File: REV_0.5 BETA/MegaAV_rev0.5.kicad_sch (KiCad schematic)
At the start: 167 parts, among them CN1 MD-90SM_MD2, P1 SMD_Conn_01x01, U1 4070, U2 74HCT123, U3 TS924, U4 THS7374, U5 ICS501, U6 TS922, U7 TS924, U8 AD725

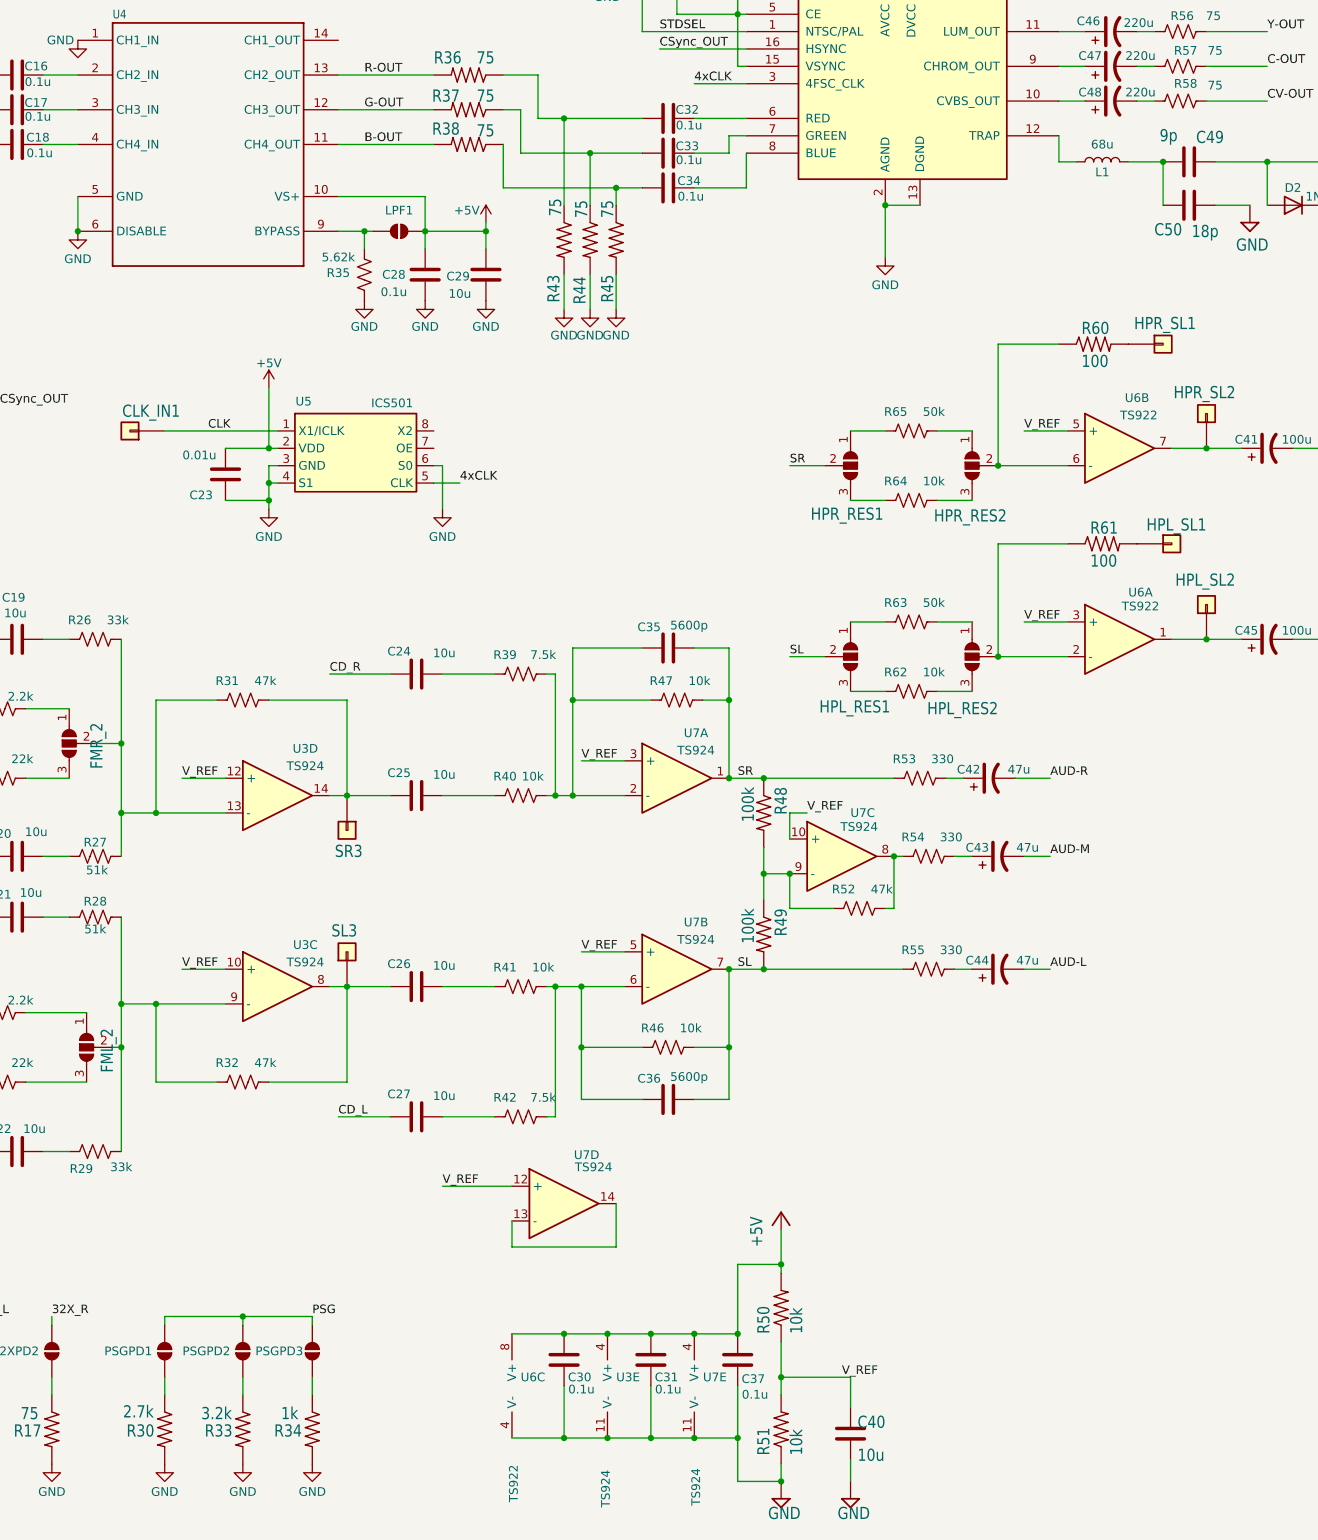
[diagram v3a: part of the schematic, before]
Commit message: optimized luma trap values & PSG fix. Some silscreening to.
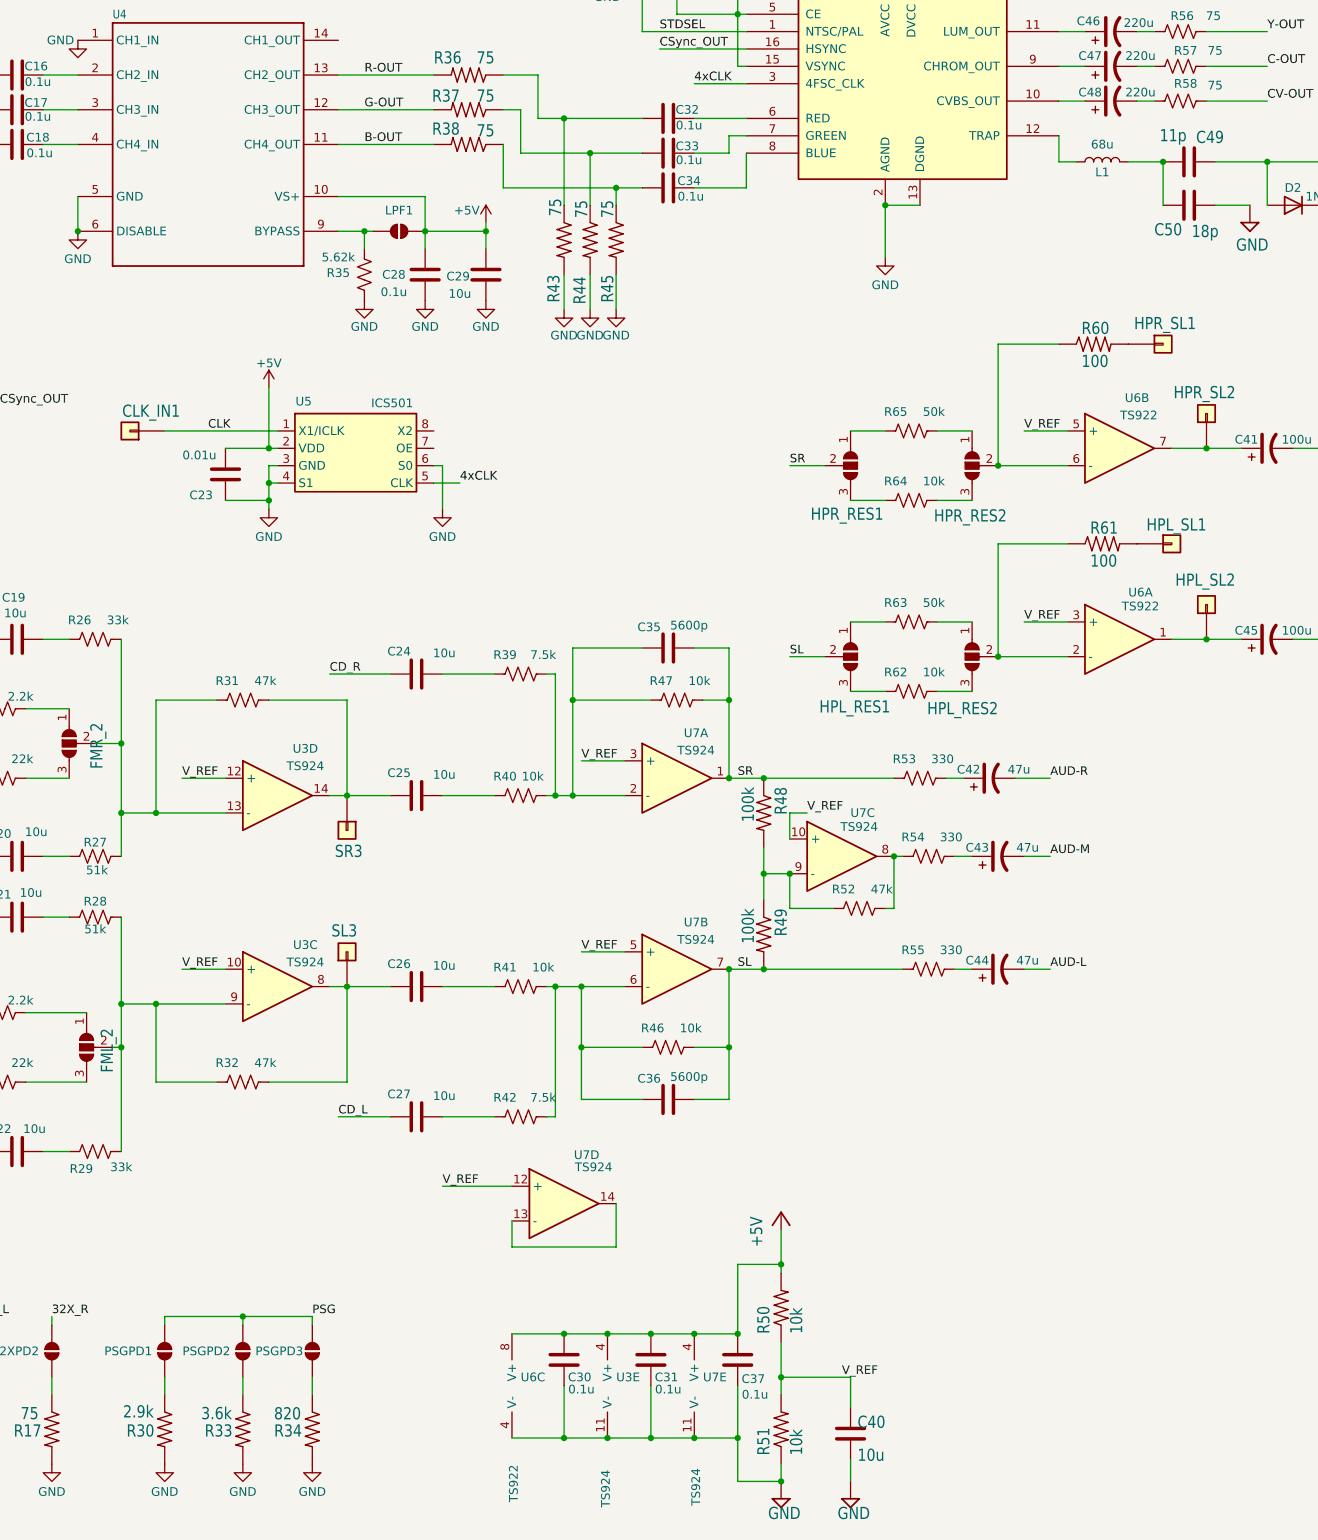
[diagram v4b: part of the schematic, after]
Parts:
- C49: value 9p -> 11p
- R30: value 2.7k -> 2.9k
- R33: value 3.2k -> 3.6k
- R34: value 1k -> 820
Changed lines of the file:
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@@
 			)
 		)
-		(property "Value" "2.7k"
+		(property "Value" "2.9k"
 			(at 174.244 247.396 90)
 			(effects
@@
 			)
 		)
-		(property "Value" "3.2k"
+		(property "Value" "3.6k"
 			(at 185.674 247.65 90)
 			(effects
@@
 			)
 		)
-		(property "Value" "9p"
+		(property "Value" "11p"
 			(at 325.882 60.706 90)
 			(effects
@@
 			)
 		)
-		(property "Value" "1k"
-			(at 197.358 247.65 90)
+		(property "Value" "820"
+			(at 196.3277 247.6768 90)
 			(effects
 				(font

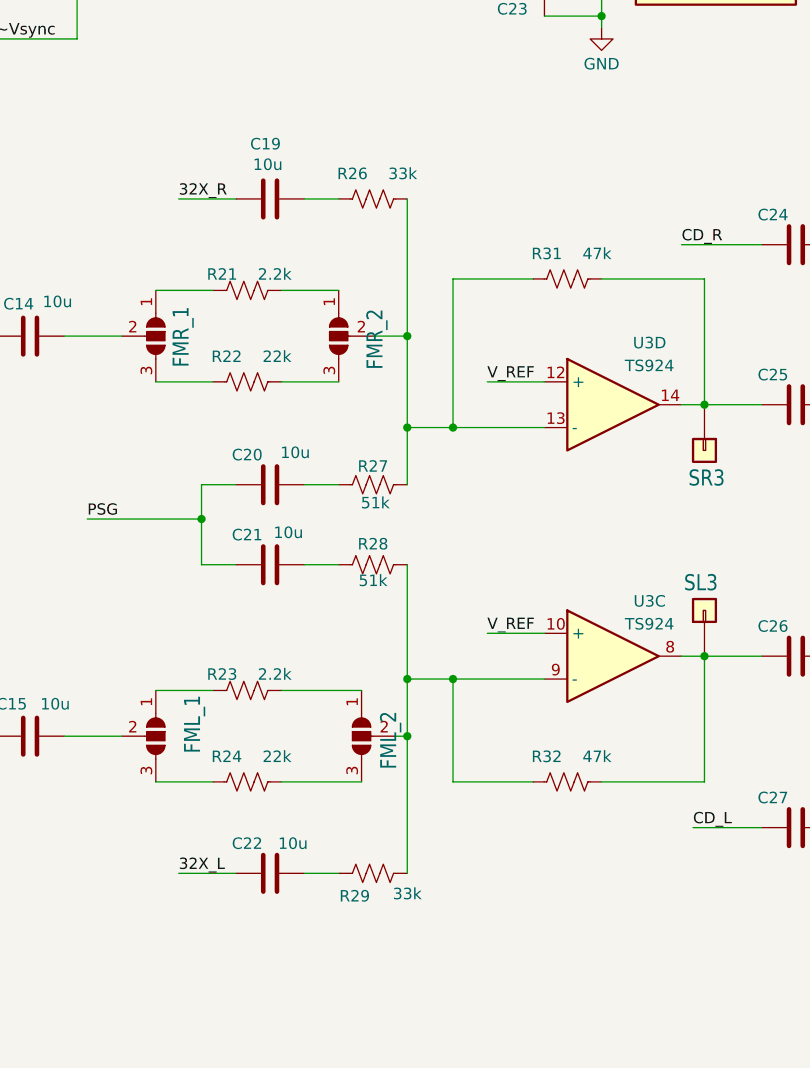
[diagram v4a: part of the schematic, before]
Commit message: 36k 32x gain fix
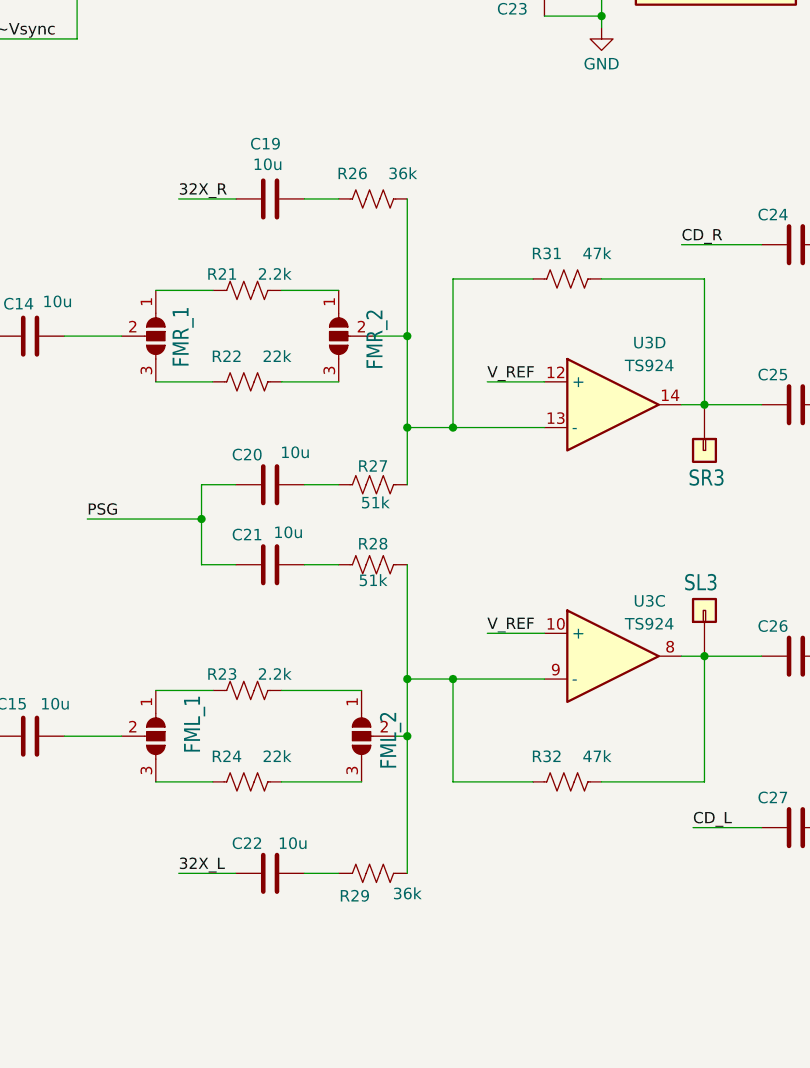
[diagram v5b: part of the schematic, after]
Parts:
- R26, R29: value 33k -> 36k
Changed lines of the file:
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@@
 			)
 		)
-		(property "Value" "33k"
+		(property "Value" "36k"
 			(at 173.482 130.556 90)
 			(effects
@@
 			)
 		)
-		(property "Value" "33k"
+		(property "Value" "36k"
 			(at 173.99 210.566 90)
 			(effects

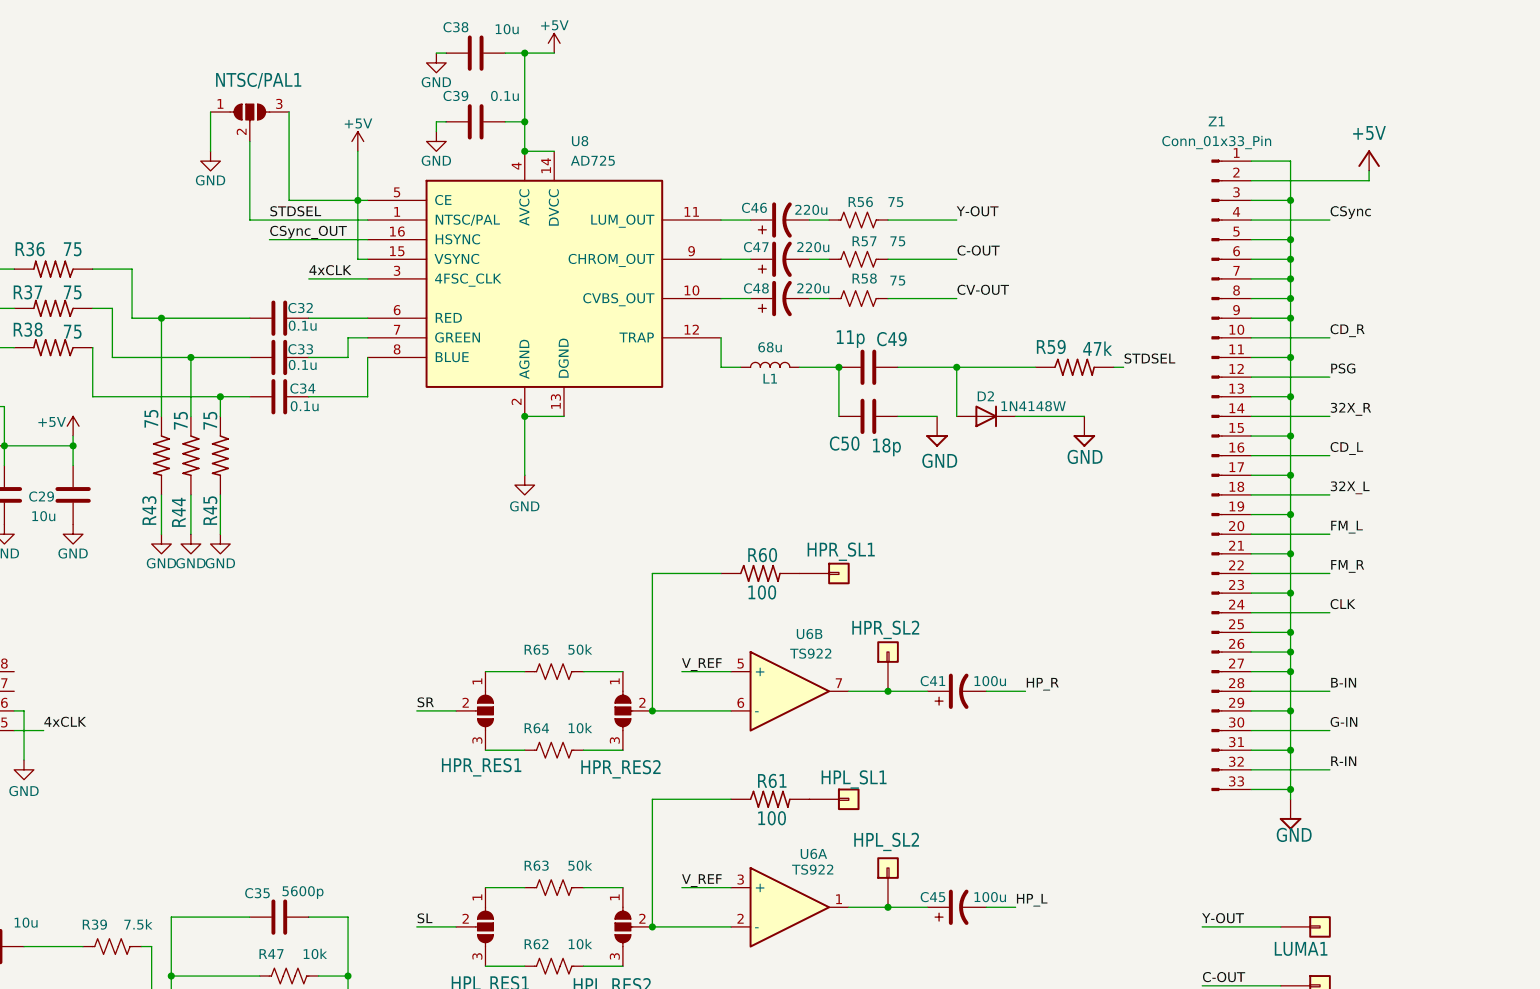
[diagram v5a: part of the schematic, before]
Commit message: Changes to the liscense, readme, and silkscreening.
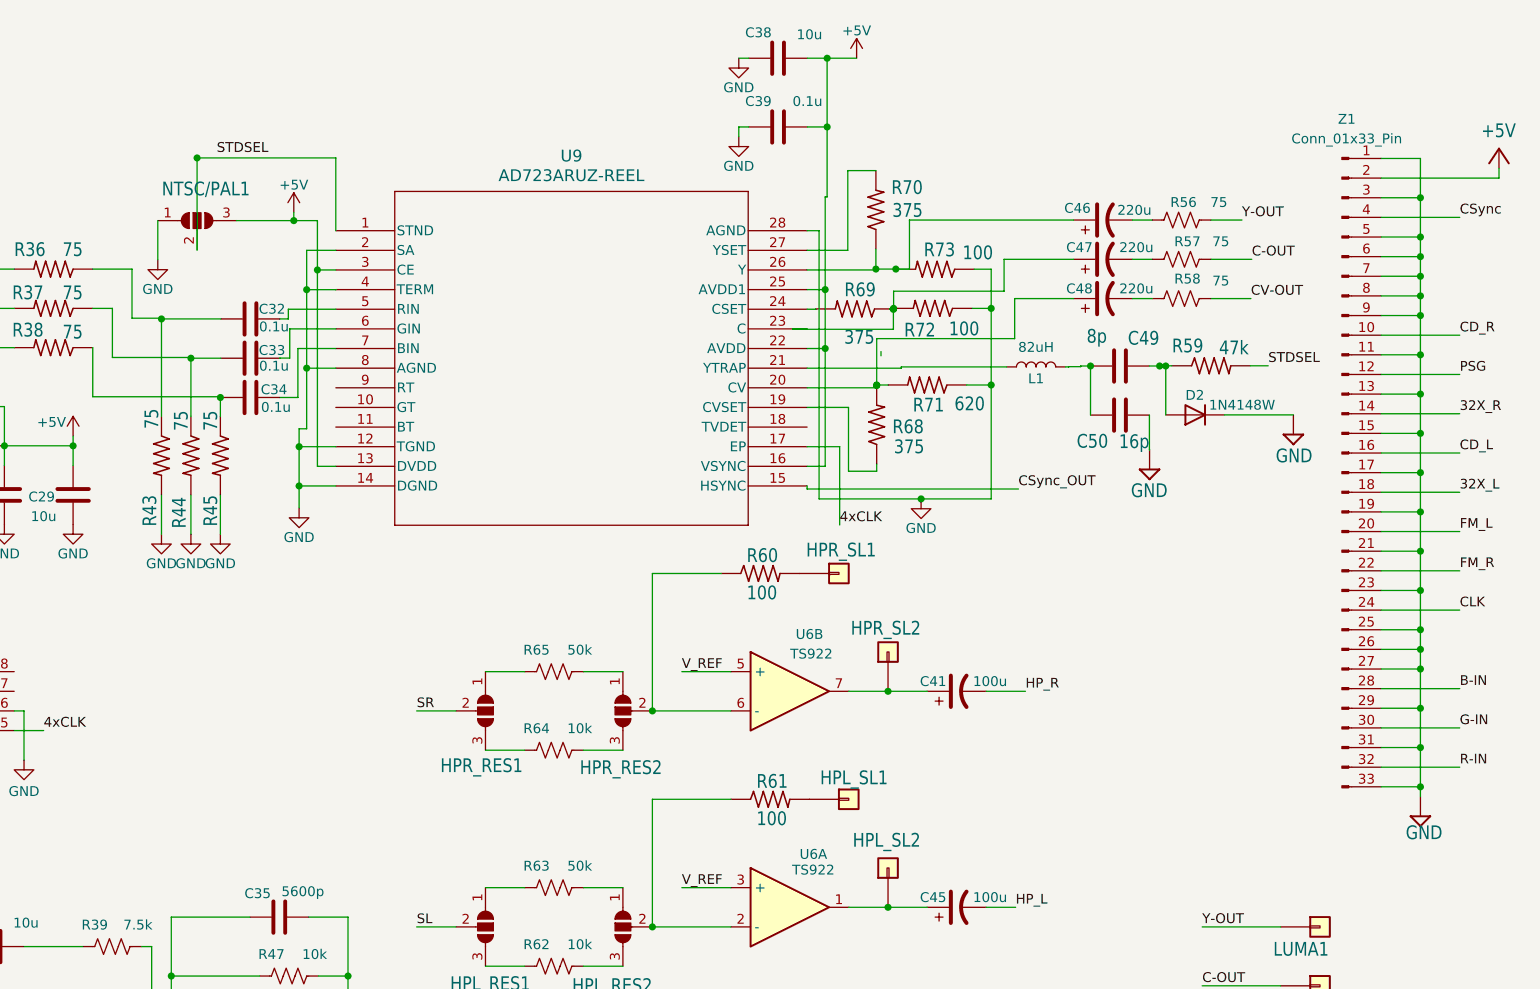
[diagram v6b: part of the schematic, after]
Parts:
- removed U8: AD725, Package_SO:SOIC-16W_7.5x10.3mm_P1.27mm, symbol Video:AD725
- added R68, R69, R70: 375, Resistor_SMD:R_0402_1005Metric, symbol 3bpV2A_RevC-eagle-import:R-US_R0603
- added R71: 620, Resistor_SMD:R_0402_1005Metric, symbol 3bpV2A_RevC-eagle-import:R-US_R0603
- added R72, R73: 100, Resistor_SMD:R_0402_1005Metric, symbol 3bpV2A_RevC-eagle-import:R-US_R0603
- added U9: AD723ARUZ-REEL, footprints:RU_28_ADI, symbol 2025-10-27_23-39-36:AD723ARUZ-REEL
- C49: value 11p -> 8p
- C50: value 18p -> 16p
- L1: value 68u -> 82uH; footprint Inductor_SMD:L_0805_2012Metric -> Inductor_SMD:L_1812_4532Metric
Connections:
- net +5V: now also U9.13 (DVDD), U9.16 (VSYNC), U9.22 (AVDD), U9.25 (AVDD1), U9.3 (CE)
- net 4xCLK: now also U9.17 (EP)
- net CSync_OUT: now also U9.15 (HSYNC)
- net GND: now also R71.1, R72.1, R73.1, U9.12 (TGND), U9.14 (DGND), U9.2 (SA), U9.28 (AGND), U9.4 (TERM), U9.8 (AGND)
- net STDSEL: no longer NTSC/PAL1.2 (C)
- net at C33.2: now also U9.6 (GIN)
- net at L1.1: now also U9.21 (YTRAP)
- net at C48.1: now also R68.2, R71.2, U9.20 (CV)
- net at C46.1: now also R70.1, R73.2, U9.26 (Y)
- net at C32.2: now also U9.5 (RIN)
- net at C34.2: now also U9.7 (BIN)
- net at C47.1: now also R69.1, R72.2, U9.23 (C)
- new net: NTSC/PAL1.2 (C), U9.1 (STND)
- new net: R68.1, U9.19 (CVSET)
- new net: R69.2, U9.24 (CSET)
- new net: R70.2, U9.27 (YSET)
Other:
- moved on the sheet: C32, C33, C34, C38, C39, C46, C47, C48, C49, C50, D2, L1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

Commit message: MEGA AV Pro & CE revisions added
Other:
- company: Developed By: Ace9921, RIP-Felix, RGBeter, Villahed94 -> Developed By:  RIP-Felix, RGBeter, Villahed94
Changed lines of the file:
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@@
 		(date "2025-07-08")
 		(rev "0.5 BETA")
-		(company "Developed By: Ace9921, RIP-Felix, RGBeter, Villahed94")
+		(company "Developed By:  RIP-Felix, RGBeter, Villahed94")
 	)
 	(junction
